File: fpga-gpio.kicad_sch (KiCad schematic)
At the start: 32 parts, among them Q5 DMG1012T-7, Q7 DMG1012T-7, Q8 DMG1012T-7, U1 MPFS250T-FCVG484, U14 NTS0102_XSON, U18 74LVC1T45GM, U19 NTS0102_XSON, U20 NTS0102_XSON, U21 NTS0102_XSON, U24 NTS0102_XSON, U25 NTS0102_XSON, U27 NTS0102_XSON, U29 NTS0102_XSON

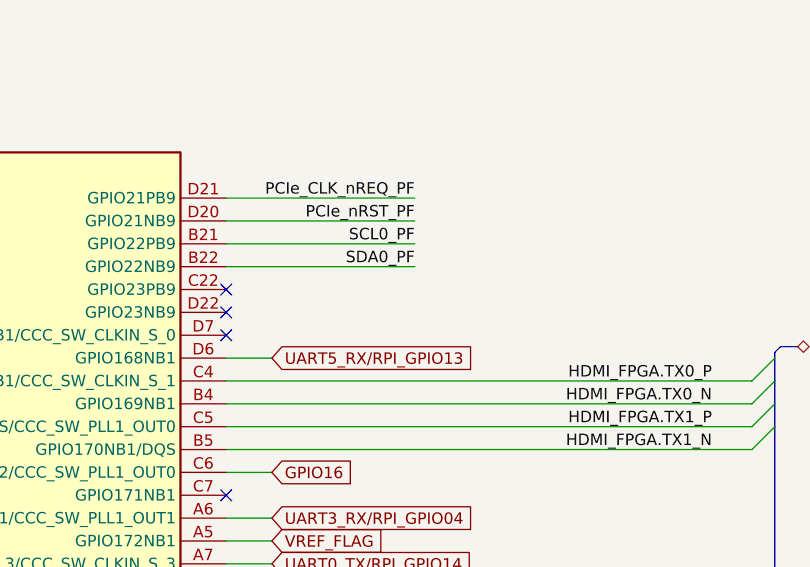
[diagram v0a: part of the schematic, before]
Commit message: [#60500] Change ULPI.RESET connection, align schematics
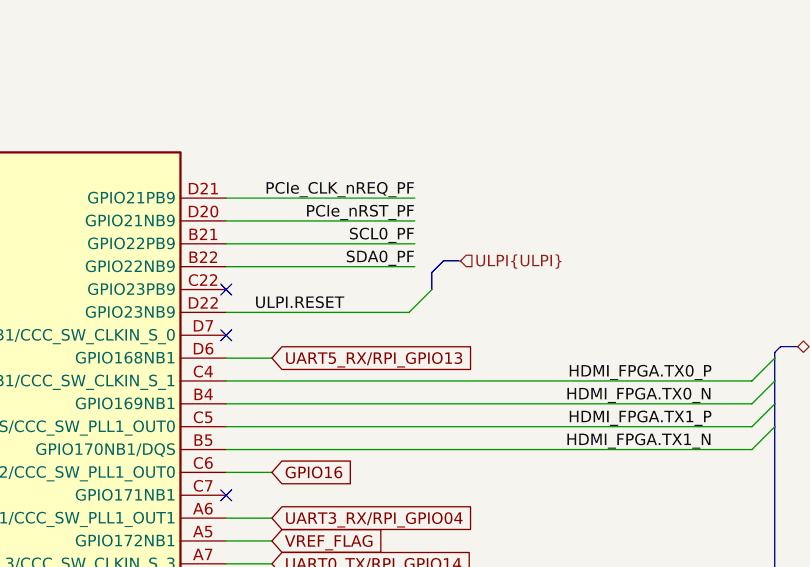
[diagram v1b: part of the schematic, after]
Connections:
- net ULPI.RESET: now reaches U1.D22 (GPIO23NB9)
- no-connect marks 16 -> 15
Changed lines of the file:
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@@
   (no_connect (at 167.64 149.86))
   (no_connect (at 76.2 93.98))
-  (no_connect (at 167.64 60.96))
   (no_connect (at 76.2 68.58))
   (no_connect (at 167.64 111.76))
@@
     (stroke (width 0) (type default))
   )
+  (bus_entry (at 187.96 60.96) (size 2.54 -2.54)
+    (stroke (width 0) (type default))
+  )
   (bus_entry (at 349.885 153.67) (size 2.54 -2.54)
     (stroke (width 0) (type default))
@@
     (stroke (width 0) (type default))
   )
+  (bus (pts (xy 190.5 56.515) (xy 190.5 58.42))
+    (stroke (width 0) (type default))
+  )
   (wire (pts (xy 367.03 222.25) (xy 367.03 223.52))
     (stroke (width 0) (type default))
@@
     (stroke (width 0) (type default))
   )
+  (bus (pts (xy 193.675 55.245) (xy 191.77 55.245))
+    (stroke (width 0) (type default))
+  )
   (wire (pts (xy 134.62 231.775) (xy 130.81 231.775))
     (stroke (width 0) (type default))
@@
     (stroke (width 0) (type default))
   )
+  (wire (pts (xy 167.64 60.96) (xy 187.96 60.96))
+    (stroke (width 0) (type default))
+  )
   (wire (pts (xy 167.64 119.38) (xy 211.455 119.38))
     (stroke (width 0) (type default))
@@
   )
   (wire (pts (xy 66.04 254) (xy 66.04 255.27))
+    (stroke (width 0) (type default))
+  )
+  (bus (pts (xy 191.77 55.245) (xy 190.5 56.515))
     (stroke (width 0) (type default))
   )
@@
     (effects (font (size 1.27 1.27)) (justify left bottom))
   )
+  (label "ULPI.RESET" (at 170.815 60.96 0) (fields_autoplaced)
+    (effects (font (size 1.27 1.27)) (justify left bottom))
+  )
   (label "PF_ETH_RESET_n" (at 290.83 227.33 0) (fields_autoplaced)
     (effects (font (size 1.27 1.27)) (justify left bottom))
@@
     (effects (font (size 1.27 1.27)) (justify right))
   )
+  (hierarchical_label "ULPI{ULPI}" (shape input) (at 193.675 55.245 0) (fields_autoplaced)
+    (effects (font (size 1.27 1.27)) (justify left))
+  )
   (hierarchical_label "ETH{SMI}" (shape input) (at 355.6 76.2 0) (fields_autoplaced)

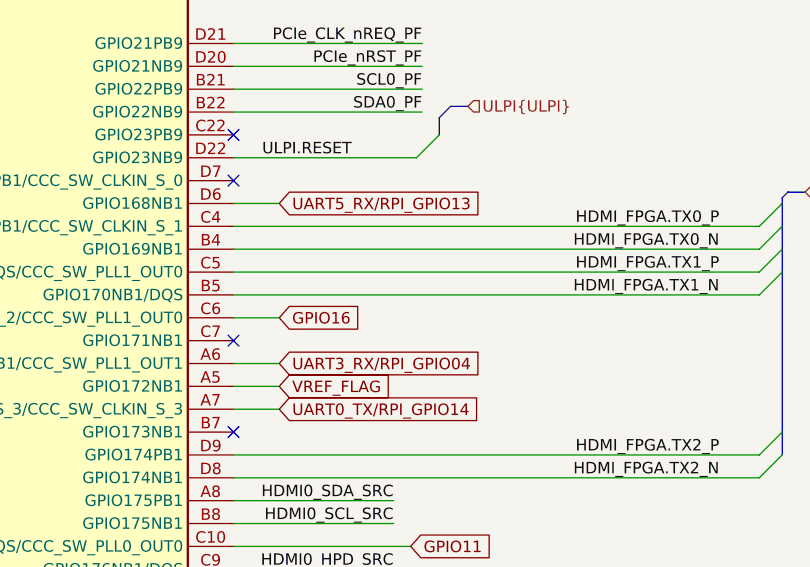
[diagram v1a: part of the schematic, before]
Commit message: [#60587] Update UART3 and UART5 nets
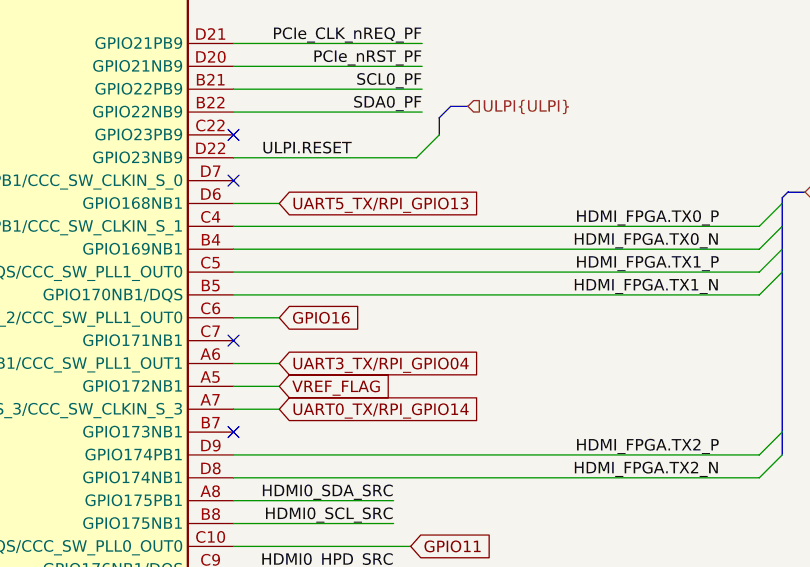
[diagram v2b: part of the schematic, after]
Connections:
- net UART3_RX/RPI_GPIO04 renamed UART3_TX/RPI_GPIO04
- net UART5_RX/RPI_GPIO13 renamed UART5_TX/RPI_GPIO13
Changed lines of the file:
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@@
     )
   )
-  (global_label "UART3_RX{slash}RPI_GPIO04" (shape input) (at 172.72 83.82 0) (fields_autoplaced)
+  (global_label "UART3_TX{slash}RPI_GPIO04" (shape input) (at 172.72 83.82 0) (fields_autoplaced)
     (effects (font (size 1.27 1.27)) (justify left))
-    (property "Intersheetrefs" "${INTERSHEET_REFS}" (at 196.7836 83.7406 0)
+    (property "Intersheetrefs" "${INTERSHEET_REFS}" (at 197.0533 83.82 0)
       (effects (font (size 1.27 1.27)) (justify left))
     )
@@
     )
   )
-  (global_label "UART5_RX{slash}RPI_GPIO13" (shape input) (at 172.72 66.04 0) (fields_autoplaced)
+  (global_label "UART5_TX{slash}RPI_GPIO13" (shape input) (at 172.72 66.04 0) (fields_autoplaced)
     (effects (font (size 1.27 1.27)) (justify left))
-    (property "Intersheetrefs" "${INTERSHEET_REFS}" (at 196.7836 65.9606 0)
+    (property "Intersheetrefs" "${INTERSHEET_REFS}" (at 197.0533 66.04 0)
       (effects (font (size 1.27 1.27)) (justify left))
     )
